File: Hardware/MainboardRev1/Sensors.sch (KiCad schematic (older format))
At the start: 25 parts, among them J6 Stratologger_PWR: 1586038-2, J7 Stratologger_DATA, Q25 SSM3J328R, Q26 NTR4003, U12 ABPMANN030PG2A3, U13 LSM9DS1, U14 LIS331HH, U15 BME280, U16 CCS811

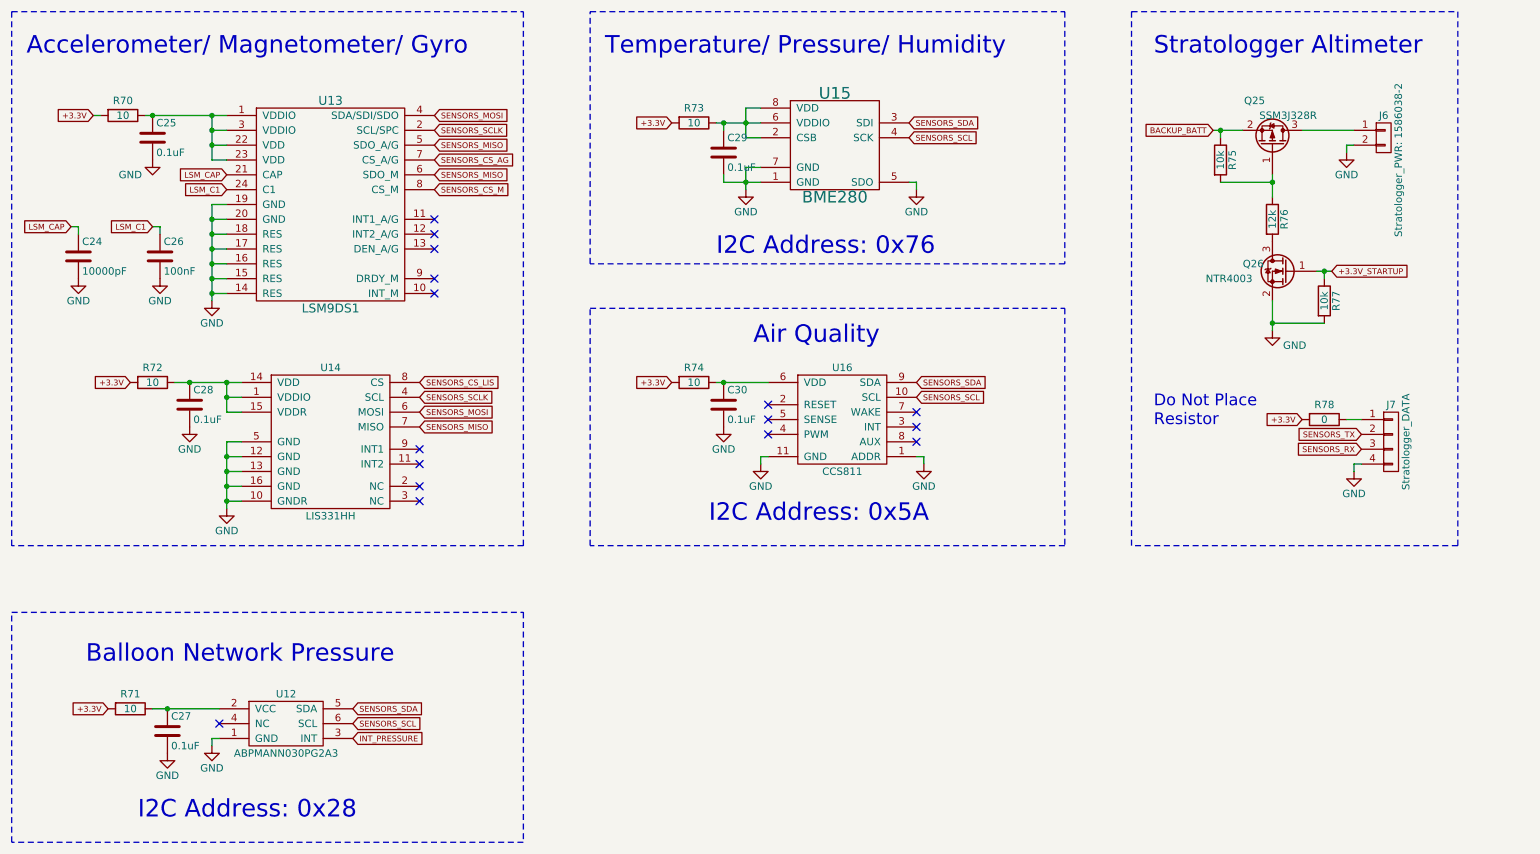
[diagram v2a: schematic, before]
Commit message: Added buzzer and strobe LED. Created BOM. Reannotated. Added sponsors to silkscreen. Needs to be routed and sent out. Good luck Matt!
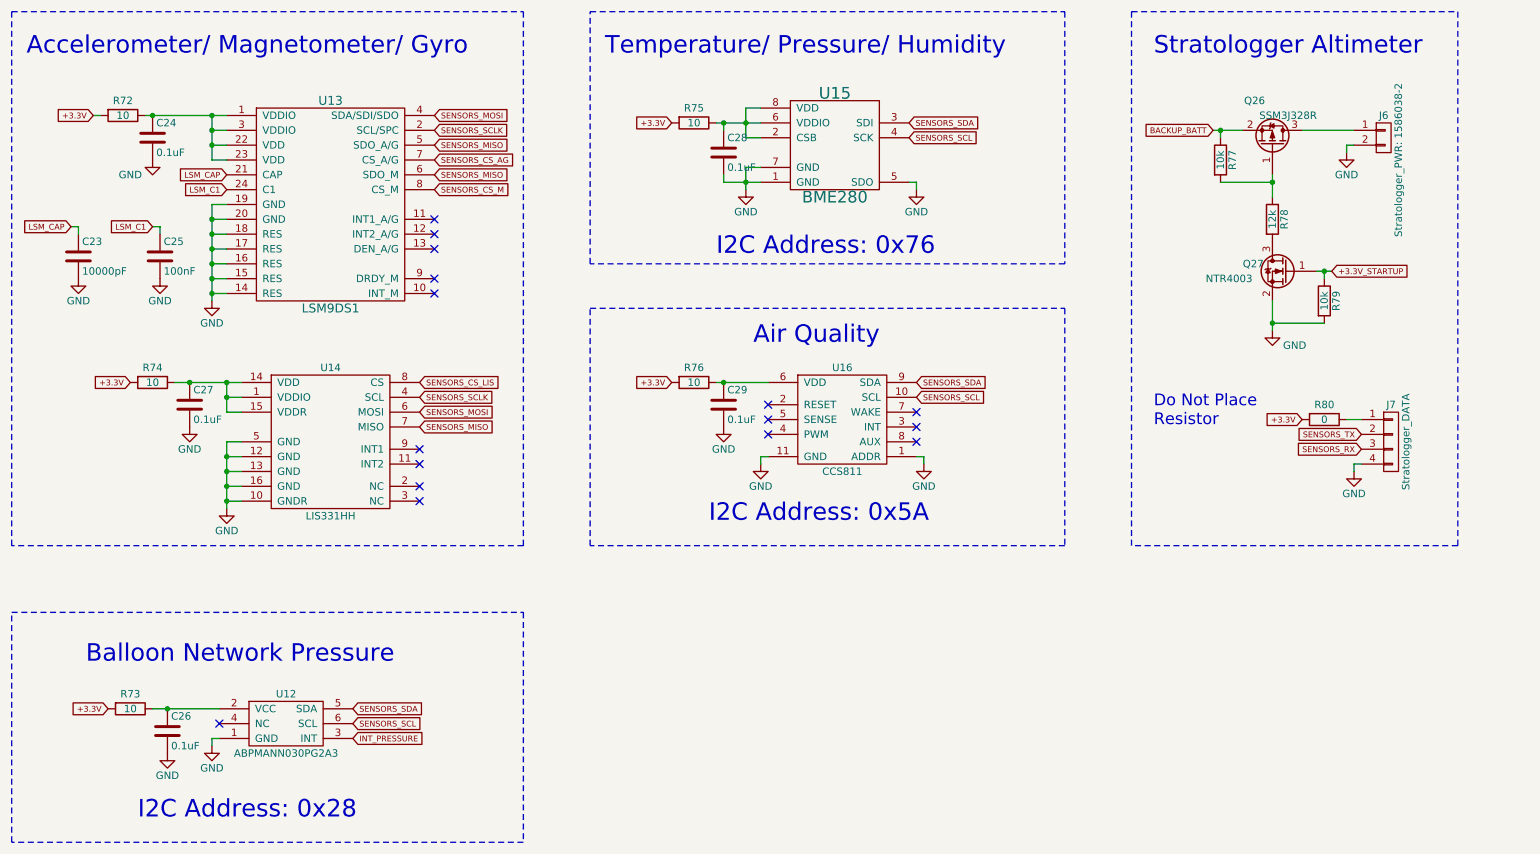
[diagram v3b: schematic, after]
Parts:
- J6: footprint Dans_Parts:CONN_2POS_VERT_TE_CONN -> Dans_Parts:CONN_2POS_VERT_TE_CONN_LOCK_5-103669-1
- renumbered C24 to C23, C25 to C24, C26 to C25, C27 to C26, C28 to C27, C29 to C28, C30 to C29, Q25 to Q26, Q26 to Q27, R70 to R72, R71 to R73, R72 to R74, R73 to R75, R74 to R76, R75 to R77, R76 to R78, R77 to R79, R78 to R80
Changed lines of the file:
@@
 +3.3V
 $Comp
-L R R70
+L R R72
 U 1 1 5AFB8442
 P 1750 1950
-F 0 "R70" V 1650 1950 50  0000 C CNN
+F 0 "R72" V 1650 1950 50  0000 C CNN
 F 1 "10" V 1750 1950 50  0000 C CNN
 F 2 "Resistors_SMD:R_0603_HandSoldering" V 1680 1950 50  0001 C CNN
@@
 $EndComp
 $Comp
-L C C25
+L C C24
 U 1 1 5AFB84A4
 P 1950 2100
-F 0 "C25" H 1975 2200 50  0000 L CNN
+F 0 "C24" H 1975 2200 50  0000 L CNN
 F 1 "0.1uF" H 1975 2000 50  0000 L CNN
 F 2 "Capacitors_SMD:C_0603_HandSoldering" H 1988 1950 50  0001 C CNN
@@
 $EndComp
 $Comp
-L GND #PWR056
+L GND #PWR054
 U 1 1 5AFB852E
 P 1950 2250
-F 0 "#PWR056" H 1950 2000 50  0001 C CNN
+F 0 "#PWR054" H 1950 2000 50  0001 C CNN
 F 1 "GND" H 1800 2150 50  0000 C CNN
 F 2 "" H 1950 2250 50  0001 C CNN
@@
 LSM_C1
 $Comp
-L GND #PWR057
+L GND #PWR055
 U 1 1 5AFB88C9
 P 2350 3200
-F 0 "#PWR057" H 2350 2950 50  0001 C CNN
+F 0 "#PWR055" H 2350 2950 50  0001 C CNN
 F 1 "GND" H 2350 3050 50  0000 C CNN
 F 2 "" H 2350 3200 50  0001 C CNN
@@
 $EndComp
 $Comp
-L C C24
+L C C23
 U 1 1 5AFB8B0C
 P 1450 2900
-F 0 "C24" H 1475 3000 50  0000 L CNN
+F 0 "C23" H 1475 3000 50  0000 L CNN
 F 1 "10000pF" H 1475 2800 50  0000 L CNN
 F 2 "Capacitors_SMD:C_0603_HandSoldering" H 1488 2750 50  0001 C CNN
@@
 $EndComp
 $Comp
-L C C26
+L C C25
 U 1 1 5AFB8B41
 P 2000 2900
-F 0 "C26" H 2025 3000 50  0000 L CNN
+F 0 "C25" H 2025 3000 50  0000 L CNN
 F 1 "100nF" H 2025 2800 50  0000 L CNN
 F 2 "Capacitors_SMD:C_0603_HandSoldering" H 2038 2750 50  0001 C CNN
@@
 $EndComp
 $Comp
-L GND #PWR058
+L GND #PWR056
 U 1 1 5AFB8B74
 P 1450 3050
-F 0 "#PWR058" H 1450 2800 50  0001 C CNN
+F 0 "#PWR056" H 1450 2800 50  0001 C CNN
 F 1 "GND" H 1450 2900 50  0000 C CNN
 F 2 "" H 1450 3050 50  0001 C CNN
@@
 $EndComp
 $Comp
-L GND #PWR059
+L GND #PWR057
 U 1 1 5AFB8B92
 P 2000 3050
-F 0 "#PWR059" H 2000 2800 50  0001 C CNN
+F 0 "#PWR057" H 2000 2800 50  0001 C CNN
 F 1 "GND" H 2000 2900 50  0000 C CNN
 F 2 "" H 2000 3050 50  0001 C CNN
@@
 $EndComp
 $Comp
-L GND #PWR060
+L GND #PWR058
 U 1 1 5AFB9518
 P 7100 2450
-F 0 "#PWR060" H 7100 2200 50  0001 C CNN
+F 0 "#PWR058" H 7100 2200 50  0001 C CNN
 F 1 "GND" H 7100 2300 50  0000 C CNN
 F 2 "" H 7100 2450 50  0001 C CNN
@@
 $EndComp
 $Comp
-L GND #PWR061
+L GND #PWR059
 U 1 1 5AFB95E4
 P 5950 2450
-F 0 "#PWR061" H 5950 2200 50  0001 C CNN
+F 0 "#PWR059" H 5950 2200 50  0001 C CNN
 F 1 "GND" H 5950 2300 50  0000 C CNN
 F 2 "" H 5950 2450 50  0001 C CNN
@@
 $EndComp
 $Comp
-L C C29
+L C C28
 U 1 1 5AFB983D
 P 5800 2200
-F 0 "C29" H 5825 2300 50  0000 L CNN
+F 0 "C28" H 5825 2300 50  0000 L CNN
 F 1 "0.1uF" H 5825 2100 50  0000 L CNN
 F 2 "Capacitors_SMD:C_0603_HandSoldering" H 5838 2050 50  0001 C CNN
@@
 $EndComp
 $Comp
-L R R73
+L R R75
 U 1 1 5AFB9924
 P 5600 2000
-F 0 "R73" V 5500 2000 50  0000 C CNN
+F 0 "R75" V 5500 2000 50  0000 C CNN
 F 1 "10" V 5600 2000 50  0000 C CNN
 F 2 "Resistors_SMD:R_0603_HandSoldering" V 5530 2000 50  0001 C CNN
@@
 NoConn ~ 3750 4450
 $Comp
-L GND #PWR062
+L GND #PWR060
 U 1 1 5AFBAE49
 P 2450 4600
-F 0 "#PWR062" H 2450 4350 50  0001 C CNN
+F 0 "#PWR060" H 2450 4350 50  0001 C CNN
 F 1 "GND" H 2450 4450 50  0000 C CNN
 F 2 "" H 2450 4600 50  0001 C CNN
@@
 $EndComp
 $Comp
-L C C28
+L C C27
 U 1 1 5AFBB438
 P 2200 3900
-F 0 "C28" H 2225 4000 50  0000 L CNN
+F 0 "C27" H 2225 4000 50  0000 L CNN
 F 1 "0.1uF" H 2225 3800 50  0000 L CNN
 F 2 "Capacitors_SMD:C_0603_HandSoldering" H 2238 3750 50  0001 C CNN
@@
 $EndComp
 $Comp
-L GND #PWR063
+L GND #PWR061
 U 1 1 5AFBB46D
 P 2200 4050
-F 0 "#PWR063" H 2200 3800 50  0001 C CNN
+F 0 "#PWR061" H 2200 3800 50  0001 C CNN
 F 1 "GND" H 2200 3900 50  0000 C CNN
 F 2 "" H 2200 4050 50  0001 C CNN
@@
 $EndComp
 $Comp
-L R R72
+L R R74
 U 1 1 5AFBB4F4
 P 1950 3750
-F 0 "R72" V 1850 3750 50  0000 C CNN
+F 0 "R74" V 1850 3750 50  0000 C CNN
 F 1 "10" V 1950 3750 50  0000 C CNN
 F 2 "Resistors_SMD:R_0603_HandSoldering" V 1880 3750 50  0001 C CNN
@@
 NoConn ~ 6100 4100
 $Comp
-L C C30
+L C C29
 U 1 1 5AFBC423
 P 5800 3900
-F 0 "C30" H 5825 4000 50  0000 L CNN
+F 0 "C29" H 5825 4000 50  0000 L CNN
 F 1 "0.1uF" H 5825 3800 50  0000 L CNN
 F 2 "Capacitors_SMD:C_0603_HandSoldering" H 5838 3750 50  0001 C CNN
@@
 	5750 3750 6100 3750
 $Comp
-L R R74
+L R R76
 U 1 1 5AFBC5C4
 P 5600 3750
-F 0 "R74" V 5500 3750 50  0000 C CNN
+F 0 "R76" V 5500 3750 50  0000 C CNN
 F 1 "10" V 5600 3750 50  0000 C CNN
 F 2 "Resistors_SMD:R_0603_HandSoldering" V 5530 3750 50  0001 C CNN
@@
 +3.3V
 $Comp
-L GND #PWR064
+L GND #PWR062
 U 1 1 5AFBC6D4
 P 5800 4050
-F 0 "#PWR064" H 5800 3800 50  0001 C CNN
+F 0 "#PWR062" H 5800 3800 50  0001 C CNN
 F 1 "GND" H 5800 3900 50  0000 C CNN
 F 2 "" H 5800 4050 50  0001 C CNN
@@
 $EndComp
 $Comp
-L GND #PWR065
+L GND #PWR063
 U 1 1 5AFBC95B
 P 6050 4300
-F 0 "#PWR065" H 6050 4050 50  0001 C CNN
+F 0 "#PWR063" H 6050 4050 50  0001 C CNN
 F 1 "GND" H 6050 4150 50  0000 C CNN
 F 2 "" H 6050 4300 50  0001 C CNN
@@
 SENSORS_SDA
 $Comp
-L GND #PWR066
+L GND #PWR064
 U 1 1 5AFBCEAE
 P 7150 4300
-F 0 "#PWR066" H 7150 4050 50  0001 C CNN
+F 0 "#PWR064" H 7150 4050 50  0001 C CNN
 F 1 "GND" H 7150 4150 50  0000 C CNN
 F 2 "" H 7150 4300 50  0001 C CNN
@@
 BACKUP_BATT
 $Comp
-L GND #PWR067
+L GND #PWR065
 U 1 1 5AFBEC0B
 P 10000 2200
-F 0 "#PWR067" H 10000 1950 50  0001 C CNN
+F 0 "#PWR065" H 10000 1950 50  0001 C CNN
 F 1 "GND" H 10000 2050 50  0000 C CNN
 F 2 "" H 10000 2200 50  0001 C CNN
@@
 F 0 "J6" H 10250 2250 50  0000 C CNN
 F 1 "Stratologger_PWR: 1586038-2" V 10350 1950 50  0000 C CNN
-F 2 "Dans_Parts:CONN_2POS_VERT_TE_CONN" H 10250 2100 50  0001 C CNN
+F 2 "Dans_Parts:CONN_2POS_VERT_TE_CONN_LOCK_5-103669-1" H 10250 2100 50  0001 C CNN
 F 3 "" H 10250 2100 50  0001 C CNN
 	1    10250 2100
@@
 $EndComp
 $Comp
-L GND #PWR068
+L GND #PWR066
 U 1 1 5AFBF3FF
 P 10050 4350
-F 0 "#PWR068" H 10050 4100 50  0001 C CNN
+F 0 "#PWR066" H 10050 4100 50  0001 C CNN
 F 1 "GND" H 10050 4200 50  0000 C CNN
 F 2 "" H 10050 4350 50  0001 C CNN
@@
 	10050 4300 10100 4300
 $Comp
-L R R78
+L R R80
 U 1 1 5AFBF69F
 P 9850 4000
-F 0 "R78" V 9750 4000 50  0000 C CNN
+F 0 "R80" V 9750 4000 50  0000 C CNN
 F 1 "0" V 9850 4000 50  0000 C CNN
 F 2 "Resistors_SMD:R_0603_HandSoldering" V 9780 4000 50  0001 C CNN
@@
 $EndComp
 $Comp
-L C C27
+L C C26
 U 1 1 5AFC1C18
 P 2050 6100
-F 0 "C27" H 2075 6200 50  0000 L CNN
+F 0 "C26" H 2075 6200 50  0000 L CNN
 F 1 "0.1uF" H 2075 6000 50  0000 L CNN
 F 2 "Capacitors_SMD:C_0603_HandSoldering" H 2088 5950 50  0001 C CNN
@@
 	1950 5950 2400 5950
 $Comp
-L GND #PWR069
+L GND #PWR067
 U 1 1 5AFC1CBA
 P 2050 6250
-F 0 "#PWR069" H 2050 6000 50  0001 C CNN
+F 0 "#PWR067" H 2050 6000 50  0001 C CNN
 F 1 "GND" H 2050 6100 50  0000 C CNN
 F 2 "" H 2050 6250 50  0001 C CNN
@@
 $EndComp
 $Comp
-L GND #PWR070
+L GND #PWR068
 U 1 1 5AFC1CF4
 P 2350 6200
-F 0 "#PWR070" H 2350 5950 50  0001 C CNN
+F 0 "#PWR068" H 2350 5950 50  0001 C CNN
 F 1 "GND" H 2350 6050 50  0000 C CNN
 F 2 "" H 2350 6200 50  0001 C CNN
@@
 	2350 6150 2400 6150
 $Comp
-L R R71
+L R R73
 U 1 1 5AFC1ECC
 P 1800 5950
-F 0 "R71" V 1700 5950 50  0000 C CNN
+F 0 "R73" V 1700 5950 50  0000 C CNN
 F 1 "10" V 1800 5950 50  0000 C CNN
 F 2 "Resistors_SMD:R_0603_HandSoldering" V 1730 5950 50  0001 C CNN
@@
 	8550 4850 8550 1250
 $Comp
-L Q_PMOS_GSD Q25
+L Q_PMOS_GSD Q26
 U 1 1 5B0149B8
 P 9500 2150
-F 0 "Q25" V 9800 2100 50  0000 R CNN
+F 0 "Q26" V 9800 2100 50  0000 R CNN
 F 1 "SSM3J328R" V 9700 2450 50  0000 R CNN
 F 2 "TO_SOT_Packages_SMD:SOT-23" H 9700 2250 50  0001 C CNN
@@
 $EndComp
 $Comp
-L GND #PWR071
+L GND #PWR069
 U 1 1 5B0149BF
 P 9500 3400
-F 0 "#PWR071" H 9500 3150 50  0001 C CNN
+F 0 "#PWR069" H 9500 3150 50  0001 C CNN
 F 1 "GND" H 9650 3300 50  0000 C CNN
 F 2 "" H 9500 3400 50  0000 C CNN
@@
 $EndComp
 $Comp
-L R R77
+L R R79
 U 1 1 5B0149C5
 P 9850 3200
-F 0 "R77" V 9930 3200 50  0000 C CNN
+F 0 "R79" V 9930 3200 50  0000 C CNN
 F 1 "10k" V 9850 3200 50  0000 C CNN
 F 2 "Resistors_SMD:R_0603_HandSoldering" V 9780 3200 50  0001 C CNN
@@
 $EndComp
 $Comp
-L Q_NMOS_GSD Q26
+L Q_NMOS_GSD Q27
 U 1 1 5B0149CC
 P 9600 3000
-F 0 "Q26" H 9900 3050 50  0000 R CNN
+F 0 "Q27" H 9900 3050 50  0000 R CNN
 F 1 "NTR4003" H 10150 2950 50  0000 R CNN
 F 2 "TO_SOT_Packages_SMD:SOT-23" H 9800 3100 50  0001 C CNN
@@
 Connection ~ 9850 3000
 $Comp
-L R R76
+L R R78
 U 1 1 5B0149DF
 P 9500 2650
-F 0 "R76" V 9580 2650 50  0000 C CNN
+F 0 "R78" V 9580 2650 50  0000 C CNN
 F 1 "12k" V 9500 2650 50  0000 C CNN
 F 2 "Resistors_SMD:R_0603_HandSoldering" V 9430 2650 50  0001 C CNN
@@
 $EndComp
 $Comp
-L R R75
+L R R77
 U 1 1 5B014FB8
 P 9150 2250
-F 0 "R75" V 9230 2250 50  0000 C CNN
+F 0 "R77" V 9230 2250 50  0000 C CNN
 F 1 "10k" V 9150 2250 50  0000 C CNN
 F 2 "Resistors_SMD:R_0603_HandSoldering" V 9080 2250 50  0001 C CNN
